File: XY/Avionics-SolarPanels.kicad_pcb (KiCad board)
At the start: 4 copper layers, 82 x 100 mm, 213 parts, among them J1 200528-0100, J2 200528-0100, Q1 NX3008NBKS, Q10 MBT2222ADW1T1, Q11 NX3008NBKS, Q12 MBT2222ADW1T1, Q13 NX3008NBKS, Q14 MBT2222ADW1T1, Q15 NX3008NBKS, Q16 MBT2222ADW1T1, Q2 MBT2222ADW1T1, Q3 NX3008NBKS, Q4 MBT2222ADW1T1, Q5 NX3008NBKS, Q6 MBT2222ADW1T1, Q7 NX3008NBKS, Q8 MBT2222ADW1T1, Q9 NX3008NBKS, U1 OPT4003DNPRQ1, U10 NCV891330PD50R2G, U11 LTC4376CDHD_PBF, U12 LTC3130, U13 LTC4376CDHD_PBF, U14 SI3865DDV-T1-GE3, U2 ADM1176-1ARMZ-R7, U3 LTC3130, U4 LTC3130, U5 DRV8830DRC, U6 ADM1176-1ARMZ-R7, U7 SI3865DDV-T1-GE3, U8 LTC4376CDHD_PBF, U9 SI3865DDV-T1-GE3

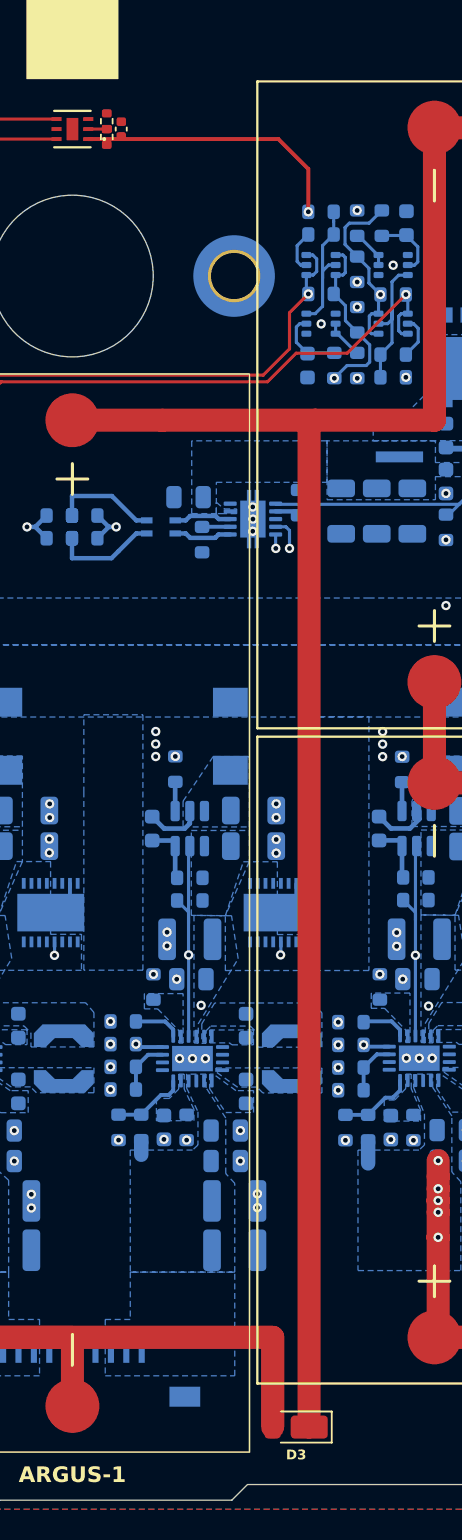
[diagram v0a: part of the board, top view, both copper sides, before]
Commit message: Added Z+ and Z- projects (WIP)
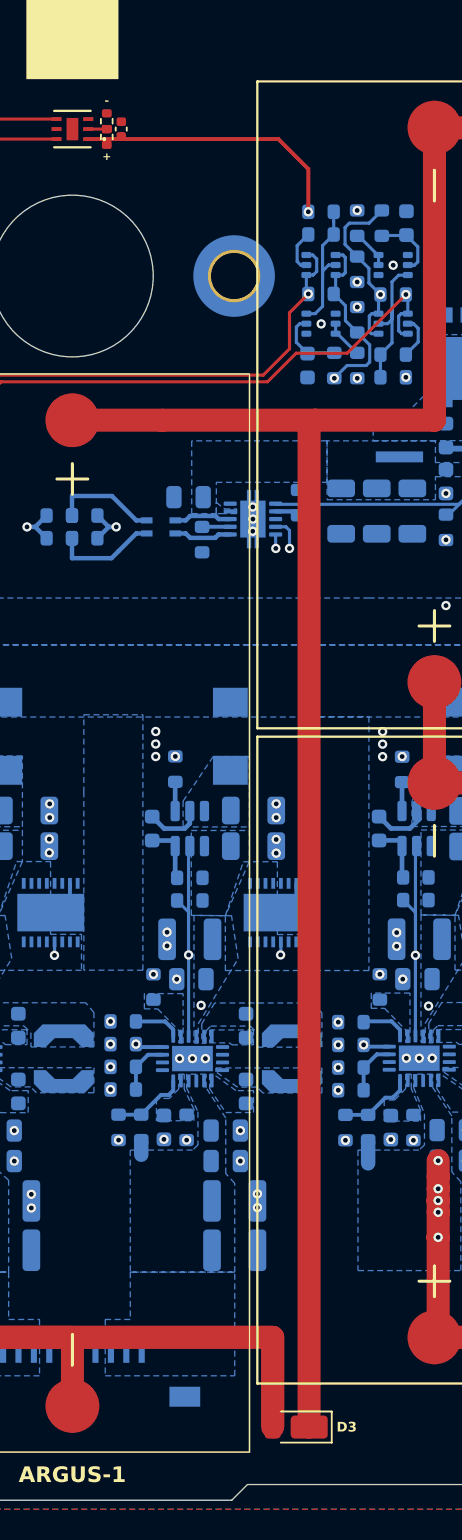
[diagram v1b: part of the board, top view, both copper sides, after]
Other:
- board text added: "+"
- board text added: "-"
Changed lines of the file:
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@@
 		(tags "PowerDI diode vishay")
 		(property "Reference" "D3"
-			(at -0.000001 -1.8034 180)
+			(at -2.6152 0 180)
 			(layer "F.SilkS")
 			(effects
@@
 					(bold yes)
 				)
+				(justify left)
 			)
 		)
@@
 			(pintype "passive")
 		)
-		(model "${KIPRJMOD}/../KiCad-Libraries/3D Models/SM141K06TF.step"
+		(model "${KIPRJMOD}/../../KiCad-Libraries/3D Models/SM141K06TF.step"
 			(offset
 				(xyz 0 0 0)
@@
 			(pintype "power_out")
 		)
-		(model "${KIPRJMOD}/../KiCad-Libraries/3D Models/OPT4003DNPRQ1.STEP"
+		(model "${KIPRJMOD}/../../KiCad-Libraries/3D Models/OPT4003DNPRQ1.STEP"
 			(offset
 				(xyz 0 0 0)
@@
 			(pintype "passive")
 		)
-		(model "${KIPRJMOD}/../KiCad-Libraries/3D Models/SM141K10TF.step"
+		(model "${KIPRJMOD}/../../KiCad-Libraries/3D Models/SM141K10TF.step"
 			(offset
 				(xyz 0 0 0)
@@
 			(pintype "passive")
 		)
-		(model "${KIPRJMOD}/../KiCad-Libraries/3D Models/SM141K06TF.step"
+		(model "${KIPRJMOD}/../../KiCad-Libraries/3D Models/SM141K06TF.step"
 			(offset
 				(xyz 0 0 0)
@@
 			(pintype "passive")
 		)
-		(model "${KIPRJMOD}/../KiCad-Libraries/3D Models/SM141K06TF.step"
+		(model "${KIPRJMOD}/../../KiCad-Libraries/3D Models/SM141K06TF.step"
 			(offset
 				(xyz 0 0 0)
@@
 			(pintype "passive")
 		)
-		(model "${KIPRJMOD}/../KiCad-Libraries/3D Models/SM141K06TF.step"
+		(model "${KIPRJMOD}/../../KiCad-Libraries/3D Models/SM141K06TF.step"
 			(offset
 				(xyz 0 0 0)
@@
 			(pintype "passive")
 		)
-		(model "${KIPRJMOD}/../KiCad-Libraries/3D Models/2005280100.stp"
+		(model "${KIPRJMOD}/../../KiCad-Libraries/3D Models/2005280100.stp"
 			(offset
 				(xyz 0 0 0)
@@
 			(pintype "passive")
 		)
-		(model "${KIPRJMOD}/../KiCad-Libraries/3D Models/srf2012a.stp"
+		(model "${KIPRJMOD}/../../KiCad-Libraries/3D Models/srf2012a.stp"
 			(offset
 				(xyz 0 0 0.6)
@@
 			(pintype "passive")
 		)
-		(model "${KIPRJMOD}/../KiCad-Libraries/3D Models/LSM115JE3_TR13.step"
+		(model "${KIPRJMOD}/../../KiCad-Libraries/3D Models/LSM115JE3_TR13.step"
 			(offset
 				(xyz 0 0 0)
@@
 			(layers "B.Cu" "B.Paste" "B.Mask")
 		)
-		(model "${KIPRJMOD}/../KiCad-Libraries/3D Models/NRVB440MFSWFT3G.step"
+		(model "${KIPRJMOD}/../../KiCad-Libraries/3D Models/NRVB440MFSWFT3G.step"
 			(offset
 				(xyz 0 0 0)
@@
 			(pintype "passive")
 		)
-		(model "${KIPRJMOD}/../KiCad-Libraries/3D Models/XGL3520.step"
+		(model "${KIPRJMOD}/../../KiCad-Libraries/3D Models/XGL3520.step"
 			(offset
 				(xyz 0 0 0)
@@
 			)
 		)
-		(model "${KIPRJMOD}/../KiCad-Libraries/3D Models/Coilcraft-LPS4018.step"
+		(model "${KIPRJMOD}/../../KiCad-Libraries/3D Models/Coilcraft-LPS4018.step"
 			(offset
 				(xyz 0 0 0)
@@
 			)
 		)
-		(model "${KIPRJMOD}/../KiCad-Libraries/3D Models/Coilcraft-LPS4018.step"
+		(model "${KIPRJMOD}/../../KiCad-Libraries/3D Models/Coilcraft-LPS4018.step"
 			(offset
 				(xyz 0 0 0)
@@
 			(pintype "passive")
 		)
-		(model "${KIPRJMOD}/../KiCad-Libraries/3D Models/LSM115JE3_TR13.step"
+		(model "${KIPRJMOD}/../../KiCad-Libraries/3D Models/LSM115JE3_TR13.step"
 			(offset
 				(xyz 0 0 0)
@@
 			)
 		)
-		(model "${KIPRJMOD}/../KiCad-Libraries/3D Models/Coilcraft-LPS4018.step"
+		(model "${KIPRJMOD}/../../KiCad-Libraries/3D Models/Coilcraft-LPS4018.step"
 			(offset
 				(xyz 0 0 0)
@@
 			(pintype "passive")
 		)
-		(model "${KIPRJMOD}/../KiCad-Libraries/3D Models/2005280100.stp"
+		(model "${KIPRJMOD}/../../KiCad-Libraries/3D Models/2005280100.stp"
 			(offset
 				(xyz 0 0 0)
@@
 			(pintype "passive")
 		)
-		(model "${KIPRJMOD}/../KiCad-Libraries/3D Models/LSM115JE3_TR13.step"
+		(model "${KIPRJMOD}/../../KiCad-Libraries/3D Models/LSM115JE3_TR13.step"
 			(offset
 				(xyz 0 0 0)
@@
 			)
 		)
+	)
+	(gr_text "-"
+		(at 154.6352 61.5188 0)
+		(layer "F.SilkS")
+		(effects
+			(font
+				(size 0.508 0.508)
+				(thickness 0.1016)
+				(bold yes)
+			)
+		)
+	)
+	(gr_text "+"
+		(at 154.6352 65.151 0)
+		(layer "F.SilkS")
+		(effects
+			(font
+				(size 0.508 0.508)
+				(thickness 0.1016)
+				(bold yes)
+			)
+		)

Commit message: Z- Board Files
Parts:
- R10, R18, R5: value R_Small -> 107K
- R12, R20, R7: value R_Small -> 1.47M
- R13, R21, R8: value R_Small -> 200K
- R17, R3, R9: value R_Small -> 1.91M
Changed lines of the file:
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@@
 		(pcbplotparams
 			(layerselection 0x00010fc_ffffffff)
-			(plot_on_all_layers_selection 0x0001000_00000000)
+			(plot_on_all_layers_selection 0x0000000_00000000)
 			(disableapertmacros no)
 			(usegerberextensions no)
@@
 		)
 		(property "Footprint" "SolarPanels:OPT4003"
-			(at 0 0 0)
+			(at 0 0 180)
 			(layer "F.Fab")
 			(hide yes)
@@
 		)
 		(property "Datasheet" "OPT4003DNPRQ1"
-			(at 0 0 0)
+			(at 0 0 180)
 			(layer "F.Fab")
 			(hide yes)
@@
 		)
 		(property "Description" ""
-			(at 0 0 0)
+			(at 0 0 180)
 			(layer "F.Fab")
 			(hide yes)
@@
 		)
 		(fp_circle
-			(center -2.0597 -0.65)
-			(end -2.0066 -0.635)
+			(center -1.9558 -1.0414)
+			(end -1.9027 -1.0264)
 			(stroke
 				(width 0.1524)
@@
 			(pintype "power_out")
 		)
-		(model "${KIPRJMOD}/../../KiCad-Libraries/3D Models/OPT4003DNPRQ1.STEP"
+		(model "${KIPRJMOD}/../KiCad-Libraries/3D Models/OPT4003DNPRQ1.STEP"
 			(offset
 				(xyz 0 0 0)
@@
 			)
 		)
-		(property "Value" "R_Small"
+		(property "Value" "1.91M"
 			(at 0 -1.43 90)
 			(layer "B.Fab")
@@
 			)
 		)
-		(property "Value" "R_Small"
+		(property "Value" "1.91M"
 			(at 0 -1.43 90)
 			(layer "B.Fab")
@@
 			)
 		)
-		(property "Value" "R_Small"
+		(property "Value" "1.47M"
 			(at 0 -1.43 0)
 			(layer "B.Fab")
@@
 			)
 		)
-		(property "Value" "R_Small"
+		(property "Value" "107K"
 			(at 0 -1.43 90)
 			(layer "B.Fab")
@@
 			)
 		)
-		(property "Value" "R_Small"
+		(property "Value" "107K"
 			(at 0 -1.43 90)
 			(layer "B.Fab")
@@
 			)
 		)
-		(property "Value" "R_Small"
+		(property "Value" "1.47M"
 			(at 0 -1.43 0)
 			(layer "B.Fab")
@@
 			)
 		)
-		(property "Value" "R_Small"
+		(property "Value" "200K"
 			(at 0 -1.43 0)
 			(layer "B.Fab")
@@
 			)
 		)
-		(property "Value" "R_Small"
+		(property "Value" "1.47M"
 			(at 0 -1.43 0)
 			(layer "B.Fab")
@@
 			)
 		)
-		(property "Value" "R_Small"
+		(property "Value" "200K"
 			(at 0 -1.43 0)
 			(layer "B.Fab")
@@
 			)
 		)
-		(property "Value" "R_Small"
+		(property "Value" "107K"
 			(at 0 -1.43 90)
 			(layer "B.Fab")
@@
 			)
 		)
-		(property "Value" "R_Small"
+		(property "Value" "200K"
 			(at 0 -1.43 0)
 			(layer "B.Fab")
@@
 			)
 		)
-		(property "Value" "R_Small"
+		(property "Value" "1.91M"
 			(at 0 -1.43 90)
 			(layer "B.Fab")

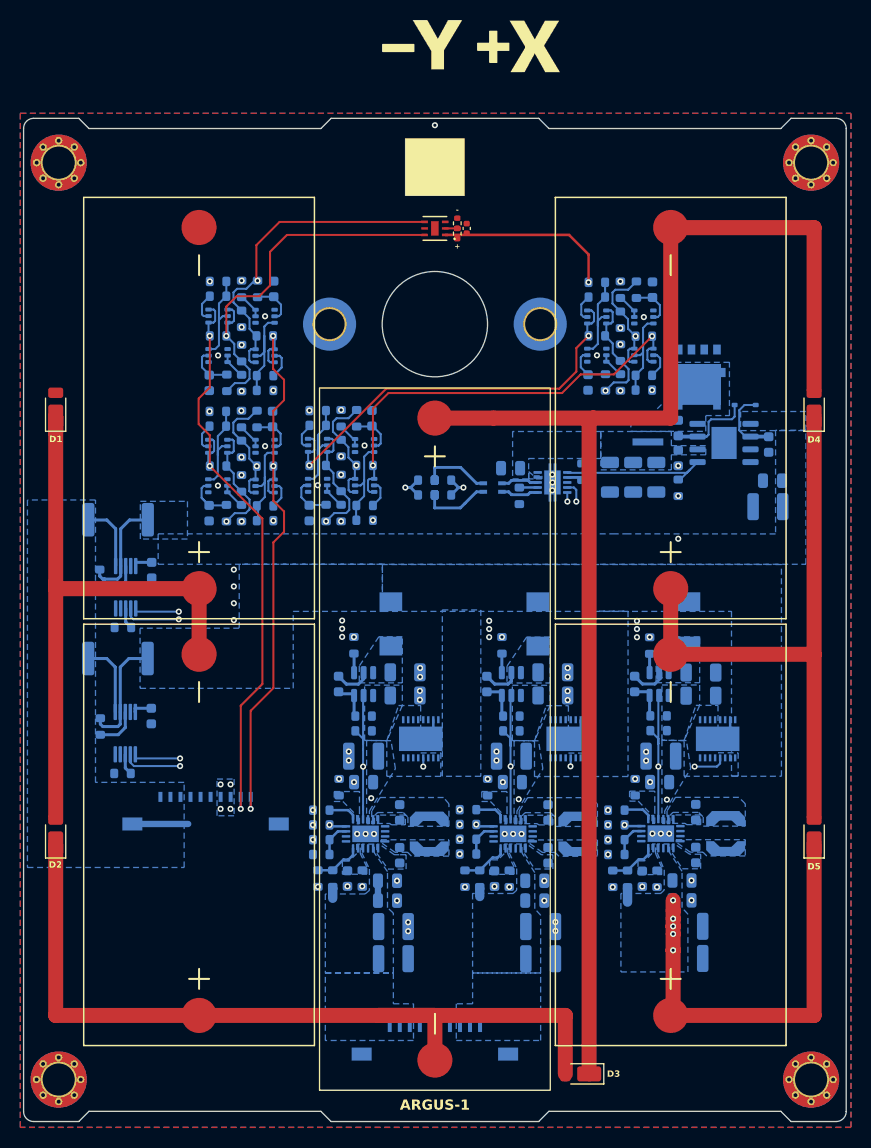
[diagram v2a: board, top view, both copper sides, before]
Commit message: Updated layout
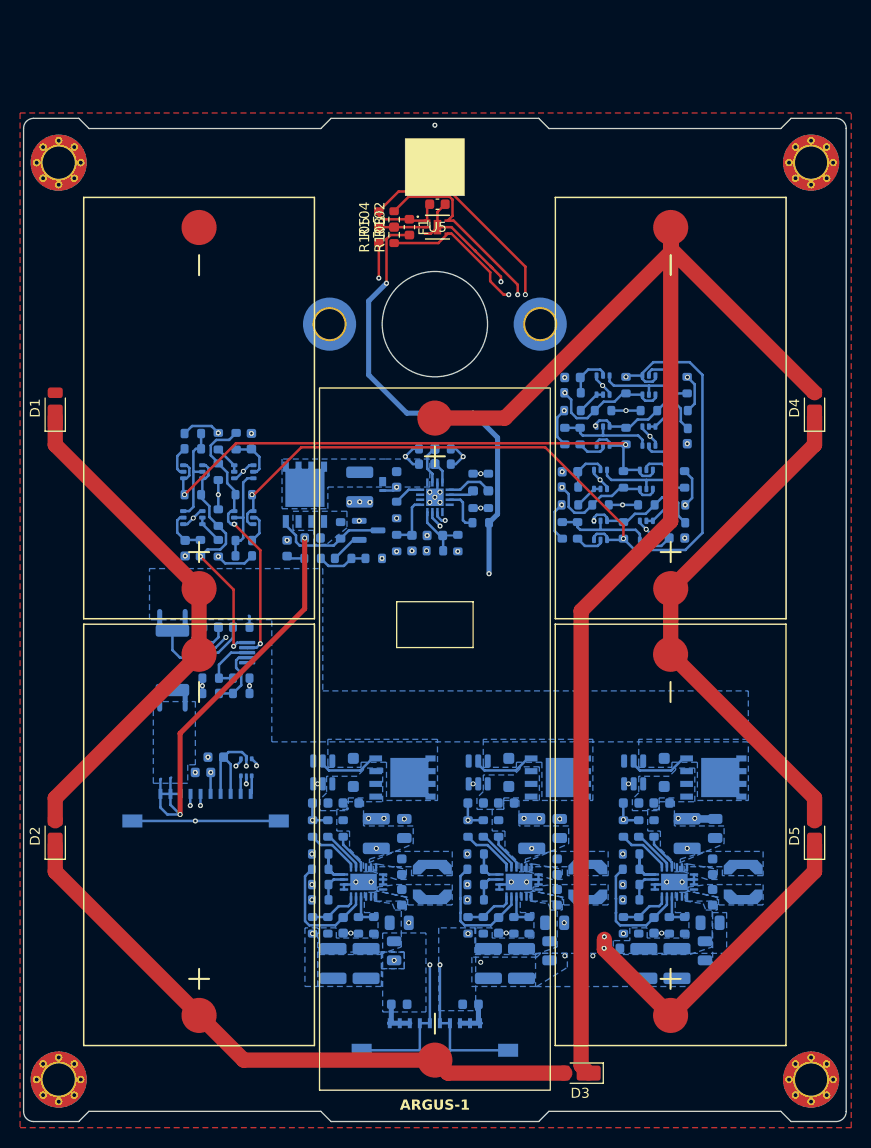
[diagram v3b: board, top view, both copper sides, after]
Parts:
- removed ?: , clipboard:eb50a26b-5fb6-463a-8dd0-ee5887daaa13
- removed C29: 3.3nF, Capacitor_SMD:C_0603_1608Metric
- removed C30, C31, C32, C33: 10nF, Capacitor_SMD:C_0603_1608Metric
- removed C50: 1uF, Capacitor_SMD:C_1206_3216Metric
- removed C51, C52, C53, C54, C55, C56: 1uF, Capacitor_SMD:C_0805_2012Metric
- removed D11: LSM115, SolarPanels:DO-214BA_MCH
- removed FL1: SRF2012, SolarPanels:SRF2012
- removed L4: XGL3520-222, SolarPanels:XGL3520
- removed Q10, Q12, Q14, Q16, Q4, Q6: MBT2222ADW1T1, Package_TO_SOT_SMD:SOT-363_SC-70-6
- removed Q11, Q13, Q15, Q3, Q5, Q9: NX3008NBKS, Package_TO_SOT_SMD:SOT-363_SC-70-6
- removed R40, R41, R47, R55, R56, R58, R65, R66, R70, R71, R75, R76, R80, R81, R91, R93: 10K, Resistor_SMD:R_0603_1608Metric
- removed R42, R57, R59, R67, R72, R77, R82: 200K, Resistor_SMD:R_0603_1608Metric
- removed R43, R63, R68, R73, R78: 680R, Resistor_SMD:R_0603_1608Metric
- removed R44, R45, R83, R84: DNI (0R), Resistor_SMD:R_0603_1608Metric
- removed R46, R64, R69, R74, R79, R90, R92: 100K, Resistor_SMD:R_0603_1608Metric
- removed R61: ?R, Resistor_SMD:R_2512_6332Metric
- removed R62: 1K, Resistor_SMD:R_0603_1608Metric
- removed REF**: , X Label
- removed Ref**: Val**, custom-footprints:ypanel
- removed U14: SI3865DDV-T1-GE3, Package_TO_SOT_SMD:SOT-23-6
- added D8: PMEG4005EH, Diode_SMD:D_SOD-123F, B.Cu at (144.3, 117.6)
- added F1: 100mA, Fuse:Fuse_0603_1608Metric, F.Cu at (149.9, 63.2)
- added F2: 500mA, Fuse:Fuse_0603_1608Metric, B.Cu at (140.2, 94.2)
- added F3: 500mA, Fuse:Fuse_0603_1608Metric, B.Cu at (175.0, 120.7)
- added F4: 500mA, Fuse:Fuse_0603_1608Metric, B.Cu at (159.5, 120.7)
- added F5: 500mA, Fuse:Fuse_0603_1608Metric, B.Cu at (144.0, 120.7)
- added F6: 100mA, Fuse:Fuse_0603_1608Metric, B.Cu at (170.1, 135.1)
- added F7: 100mA, Fuse:Fuse_0603_1608Metric, B.Cu at (156.0, 140.7)
- added F8: 100mA, Fuse:Fuse_0603_1608Metric, B.Cu at (148.8, 140.7)
- added Q17: NX3008NBKS, Package_TO_SOT_SMD:SOT-363_SC-70-6, B.Cu at (173.5, 93.5)
- added Q18: MBT2222ADW1T1, Package_TO_SOT_SMD:SOT-363_SC-70-6, B.Cu at (168.9, 93.5)
- added Q19: NX3008NBKS, Package_TO_SOT_SMD:SOT-363_SC-70-6, B.Cu at (169.2, 79.0)
- added Q20: MBT2222ADW1T1, Package_TO_SOT_SMD:SOT-363_SC-70-6, B.Cu at (173.7, 79.0)
- added Q21: NX3008NBKS, Package_TO_SOT_SMD:SOT-363_SC-70-6, B.Cu at (173.7, 84.1)
- added Q22: MBT2222ADW1T1, Package_TO_SOT_SMD:SOT-363_SC-70-6, B.Cu at (169.2, 84.1)
- added Q23: NX3008NBKS, Package_TO_SOT_SMD:SOT-363_SC-70-6, B.Cu at (133.3, 87.6)
- added Q24: MBT2222ADW1T1, Package_TO_SOT_SMD:SOT-363_SC-70-6, B.Cu at (133.3, 92.2)
- added Q25: NX3008NBKS, Package_TO_SOT_SMD:SOT-363_SC-70-6, B.Cu at (128.3, 92.2)
- added Q26: MBT2222ADW1T1, Package_TO_SOT_SMD:SOT-363_SC-70-6, B.Cu at (128.3, 87.6)
- added R100: 10K, Resistor_SMD:R_0603_1608Metric, B.Cu at (173.5, 90.9)
- added R101: 200K, Resistor_SMD:R_0603_1608Metric, B.Cu at (176.5, 92.7)
- added R102: 0R, Resistor_SMD:R_0603_1608Metric, F.Cu at (148.3, 62.5)
- added R103: 0R, Resistor_SMD:R_0603_1608Metric, F.Cu at (148.3, 64.0)
- added R104: 0R, Resistor_SMD:R_0603_1608Metric, F.Cu at (146.8, 62.5)
- added R105: 0R, Resistor_SMD:R_0603_1608Metric, F.Cu at (146.8, 64.0)
- added R106: 680R, Resistor_SMD:R_0603_1608Metric, B.Cu at (176.0, 79.0)
- added R107: 100K, Resistor_SMD:R_0603_1608Metric, B.Cu at (166.1, 81.5)
- added R108: 1.47M, Resistor_SMD:R_0603_1608Metric, B.Cu at (141.0, 128.8)
- added R109: 200K, Resistor_SMD:R_0603_1608Metric, B.Cu at (141.0, 130.3)
- added R110: 0R, Resistor_SMD:R_0603_1608Metric, B.Cu at (133.1, 108.2)
- added R111: 0R, Resistor_SMD:R_0603_1608Metric, B.Cu at (130.0, 108.2)
- added R112: 0R, Resistor_SMD:R_0603_1608Metric, B.Cu at (133.1, 109.7)
- added R113: 0R, Resistor_SMD:R_0603_1608Metric, B.Cu at (130.0, 109.7)
- added R114: DNI (0R), Resistor_SMD:R_0603_1608Metric, B.Cu at (171.4, 79.0)
- added R115: 10K, Resistor_SMD:R_0603_1608Metric, B.Cu at (177.5, 79.0)
- added R116: 10K, Resistor_SMD:R_0603_1608Metric, B.Cu at (169.2, 81.5)
- added R117: 200K, Resistor_SMD:R_0603_1608Metric, B.Cu at (166.1, 79.8)
- added R118: 680R, Resistor_SMD:R_0603_1608Metric, B.Cu at (166.9, 84.1)
- added R119: 100K, Resistor_SMD:R_0603_1608Metric, B.Cu at (176.8, 81.5)
- added R120: DNI (0R), Resistor_SMD:R_0603_1608Metric, B.Cu at (171.4, 84.1)
- added R121: 10K, Resistor_SMD:R_0603_1608Metric, B.Cu at (165.4, 84.1)
- added R122: 10K, Resistor_SMD:R_0603_1608Metric, B.Cu at (173.7, 81.5)
- added R123: 200K, Resistor_SMD:R_0603_1608Metric, B.Cu at (176.8, 83.3)
- added R124: ?R, Resistor_SMD:R_2512_6332Metric, B.Cu at (126.2, 106.4)
- added R125: 1K, Resistor_SMD:R_0603_1608Metric, B.Cu at (133.1, 103.1)
- added R126: 680R, Resistor_SMD:R_0603_1608Metric, B.Cu at (133.3, 94.5)
- added R127: 100K, Resistor_SMD:R_0603_1608Metric, B.Cu at (130.8, 84.6)
- added R128: DNI (0R), Resistor_SMD:R_0603_1608Metric, B.Cu at (133.3, 89.9)
- added R129: 10K, Resistor_SMD:R_0603_1608Metric, B.Cu at (133.3, 96.0)
- added R130: 10K, Resistor_SMD:R_0603_1608Metric, B.Cu at (130.8, 87.6)
- added R131: 200K, Resistor_SMD:R_0603_1608Metric, B.Cu at (132.6, 84.6)
- added R132: 680R, Resistor_SMD:R_0603_1608Metric, B.Cu at (128.3, 85.3)
- added R133: 100K, Resistor_SMD:R_0603_1608Metric, B.Cu at (130.8, 95.2)
- added R134: DNI (0R), Resistor_SMD:R_0603_1608Metric, B.Cu at (128.3, 89.9)
- added R135: 10K, Resistor_SMD:R_0603_1608Metric, B.Cu at (128.3, 83.8)
- added R136: 10K, Resistor_SMD:R_0603_1608Metric, B.Cu at (130.8, 92.2)
- added R137: 200K, Resistor_SMD:R_0603_1608Metric, B.Cu at (129.0, 95.2)
- added R97: 100K, Resistor_SMD:R_0603_1608Metric, B.Cu at (176.5, 90.9)
- added R98: DNI (0R), Resistor_SMD:R_0603_1608Metric, B.Cu at (171.2, 93.5)
- added R99: 10K, Resistor_SMD:R_0603_1608Metric, B.Cu at (165.1, 93.5)
- C1: value 47uF -> 0.1uF; footprint Capacitor_SMD:C_1210_3225Metric -> Capacitor_SMD:C_0603_1608Metric
- C10: value 1uF -> 4.7uF; footprint Capacitor_SMD:C_0805_2012Metric -> Capacitor_SMD:C_0603_1608Metric
- C11: value 22nF -> 1uF; footprint Capacitor_SMD:C_0603_1608Metric -> Capacitor_SMD:C_0805_2012Metric
- C12, C4: value 22nF -> 47uF; footprint Capacitor_SMD:C_0603_1608Metric -> Capacitor_SMD:C_1210_3225Metric
- C13: value 4.7uF -> 47uF; footprint Capacitor_SMD:C_0603_1608Metric -> Capacitor_SMD:C_1210_3225Metric
- C14: value 47uF -> 10uF
- C15, C7: value 47uF -> 1uF; footprint Capacitor_SMD:C_1210_3225Metric -> Capacitor_SMD:C_0805_2012Metric
- C16: value 10uF -> 1uF; footprint Capacitor_SMD:C_1210_3225Metric -> Capacitor_SMD:C_0805_2012Metric
- C17: value 1uF -> 22nF; footprint Capacitor_SMD:C_0805_2012Metric -> Capacitor_SMD:C_0603_1608Metric
- C19: value 22nF -> 4.7uF
- C2: value 10uF -> 0.1uF; footprint Capacitor_SMD:C_1210_3225Metric -> Capacitor_SMD:C_0603_1608Metric
- C20, C6: value 4.7uF -> 1uF; footprint Capacitor_SMD:C_0603_1608Metric -> Capacitor_SMD:C_0805_2012Metric
- C22: value 3.3nF -> 1nF
- C23: value 0.1uF -> 47uF; footprint Capacitor_SMD:C_0402_1005Metric -> Capacitor_SMD:C_1210_3225Metric; moved to B.Cu
- C24, C25: value 10nF -> 100nF
- C26: value 10nF -> 10uF; footprint Capacitor_SMD:C_0603_1608Metric -> Capacitor_SMD:C_1210_3225Metric
- C27: value 10nF -> 0.1uF
- C28: footprint Capacitor_SMD:C_0805_2012Metric -> Capacitor_SMD:C_0603_1608Metric
- C3: value 1uF -> 0.1uF; footprint Capacitor_SMD:C_0805_2012Metric -> Capacitor_SMD:C_0603_1608Metric
- C34: value 1uF -> 10nF; footprint Capacitor_SMD:C_0805_2012Metric -> Capacitor_SMD:C_0603_1608Metric
- C35: value 4.7uF -> 10nF; footprint Capacitor_SMD:C_1210_3225Metric -> Capacitor_SMD:C_0603_1608Metric
- C36: moved to F.Cu
- C37: value 0.1uF -> 10nF
- C38, C48: value 10uF -> 10nF; footprint Capacitor_SMD:C_1206_3216Metric -> Capacitor_SMD:C_0603_1608Metric
- C39: value 0.1uF -> 10uF; footprint Capacitor_SMD:C_0603_1608Metric -> Capacitor_SMD:C_1210_3225Metric
- C40, C41, C45: value 10uF -> 1uF; footprint Capacitor_SMD:C_1206_3216Metric -> Capacitor_SMD:C_0805_2012Metric
- C42: value 10uF -> 22nF; footprint Capacitor_SMD:C_1206_3216Metric -> Capacitor_SMD:C_0603_1608Metric
- C43: value 1nF -> 22nF
- C44: value 1uF -> 4.7uF; footprint Capacitor_SMD:C_1206_3216Metric -> Capacitor_SMD:C_0603_1608Metric
- C46: value 1nF -> 47uF; footprint Capacitor_SMD:C_0603_1608Metric -> Capacitor_SMD:C_1210_3225Metric
- C47: value 1uF -> 3.3nF; footprint Capacitor_SMD:C_1206_3216Metric -> Capacitor_SMD:C_0603_1608Metric
- C49: value 1nF -> 10nF
- C5: value 22nF -> 10uF; footprint Capacitor_SMD:C_0603_1608Metric -> Capacitor_SMD:C_1210_3225Metric
- C8: value 47uF -> 22nF; footprint Capacitor_SMD:C_1210_3225Metric -> Capacitor_SMD:C_0603_1608Metric
- C9: value 10uF -> 22nF; footprint Capacitor_SMD:C_1210_3225Metric -> Capacitor_SMD:C_0603_1608Metric
- D10: value NRVB440MFS -> 10V; footprint SolarPanels:NRVB440MFSWFT1G -> Diode_SMD:Nexperia_DSN1608-2_1.6x0.8mm
- D6, D7: value LSM115 -> PMEG4005EH; footprint SolarPanels:DO-214BA_MCH -> Diode_SMD:D_SOD-123F
- D9: value BAS16HT1G -> GREEN; footprint Diode_SMD:D_SOD-323 -> LED_SMD:LED_0603_1608Metric
- Q1: value NX3008NBKS -> IRLML2803; footprint Package_TO_SOT_SMD:SOT-363_SC-70-6 -> Package_TO_SOT_SMD:SOT-23
- Q2: value MBT2222ADW1T1 -> SIRA99DP-T1-GE3; footprint Package_TO_SOT_SMD:SOT-363_SC-70-6 -> Package_SO:PowerPAK_SO-8_Single
- R1: value 0R -> 0R (DNI)
- R10: value 107K -> 0R
- R11, R49, R54, R6: value 100K -> 0R
- R12, R7: value 1.47M -> 0R
- R13: value 200K -> 1.91M
- R14: value 0R (DNI) -> 1.91M
- R15, R16: value 0R -> 1.91M
- R17: value 1.91M -> 107K
- R18: value 107K -> 1.91M
- R19: value 100K -> 107K
- R2: value 0R (DNI) -> 0R
- R20: value 1.47M -> 1.91M
- R21: value 200K -> 107K
- R22: value 0R (DNI) -> 127k
- R23, R24: value 0R -> 127k
- R25, R26, R27: value 0R -> 100K
- R3: value 1.91M -> 0R
- R32: value ?R -> TBD; footprint Resistor_SMD:R_2512_6332Metric -> Resistor_SMD:R_0603_1608Metric
- R33: value 1K -> 10k
- R34: value 0R -> 1.47M; footprint Resistor_SMD:R_0402_1005Metric -> Resistor_SMD:R_0603_1608Metric; moved to B.Cu
- R35: value 0R -> 200K; footprint Resistor_SMD:R_0402_1005Metric -> Resistor_SMD:R_0603_1608Metric; moved to B.Cu
- R36: value 680R -> 2.7k
- R37: value 100K -> 10k
- R38: value DNI (0R) -> 10k
- R39: value DNI (0R) -> 4k7
- R48: value 680R -> 0R
- R5: value 107K -> 0R (DNI)
- R50, R51: value 10K -> 0R
- R52: value 200K -> TBD
- R53: value 680R -> TBD
- R60, R96: value 0R -> 680R
- R8: value 200K -> 0R
- R85: value DNI (0R) -> 100K
- R86: value DNI (0R) -> 10K
- R88: value 100K -> 1.47M
- R89: value 10K -> 200K
- R9: value 1.91M -> 0R (DNI)
- R94: value 0R -> 200K
- R95: value 0R -> DNI (0R)
- U1: value OPT4003DNPRQ1 -> LTC4412xS6; footprint SolarPanels:OPT4003 -> Package_TO_SOT_SMD:TSOT-23-6; moved to B.Cu
- U10: value NCV891330PD50R2G -> LTC3130; footprint Package_SO:SOIC-8-1EP_3.9x4.9mm_P1.27mm_EP2.514x3.2mm -> Package_DFN_QFN:QFN-20-1EP_3x4mm_P0.5mm_EP1.65x2.65mm
- U11: value LTC4376CDHD_PBF -> LTC3130; footprint Package_DFN_QFN:DFN-16-1EP_4x5mm_P0.5mm_EP2.44x4.34mm -> Package_DFN_QFN:QFN-20-1EP_3x4mm_P0.5mm_EP1.65x2.65mm
- U13: value LTC4376CDHD_PBF -> ADM1176-1ARMZ-R7; footprint Package_DFN_QFN:DFN-16-1EP_4x5mm_P0.5mm_EP2.44x4.34mm -> Package_SO:MSOP-10_3x3mm_P0.5mm
- U2: value ADM1176-1ARMZ-R7 -> DRV8235RTER; footprint Package_SO:MSOP-10_3x3mm_P0.5mm -> SolarPanels:WQFN16_RTE_TEX
- U3: value LTC3130 -> CSD25402Q3A; footprint Package_DFN_QFN:QFN-20-1EP_3x4mm_P0.5mm_EP1.65x2.65mm -> Package_SO:PowerPAK_SO-8_Single
- U4: value LTC3130 -> LTC4412xS6; footprint Package_DFN_QFN:QFN-20-1EP_3x4mm_P0.5mm_EP1.65x2.65mm -> Package_TO_SOT_SMD:TSOT-23-6
- U5: value DRV8830DRC -> OPT4003DNPRQ1; footprint Package_SON:VSON-10-1EP_3x3mm_P0.5mm_EP1.65x2.4mm -> SolarPanels:OPT4003; moved to F.Cu
- U6: value ADM1176-1ARMZ-R7 -> USBLC6-2P6; footprint Package_SO:MSOP-10_3x3mm_P0.5mm -> Package_TO_SOT_SMD:SOT-666
- U7, U9: value SI3865DDV-T1-GE3 -> CSD25402Q3A; footprint Package_TO_SOT_SMD:SOT-23-6 -> Package_SO:PowerPAK_SO-8_Single
- U8: value LTC4376CDHD_PBF -> LTC4412xS6; footprint Package_DFN_QFN:DFN-16-1EP_4x5mm_P0.5mm_EP2.44x4.34mm -> Package_TO_SOT_SMD:TSOT-23-6
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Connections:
- net /coil renamed /Coil Driver/coil
- C1 pad 1: VSOLAR -> Net-(D6-A)
- C10 pad 1: D_VSOLAR1 -> /Solar Charger/MPPT/VCC
- C11 pad 1: Net-(U3-SW1) -> /Solar Charger/Charge OR-ing/IN
- C11 pad 2: Net-(U3-BST1) -> GND
- C12 pad 1: Net-(U3-BST2) -> /Solar Charger/Charge OR-ing/IN
- C12 pad 2: Net-(U3-SW2) -> GND
- C13 pad 1: /MPPT1/VCC -> /Solar Charger/MPPT1/VIN
- C14 pad 1: /Charge OR-ing1/IN -> /Solar Charger/MPPT1/VIN
- C15 pad 1: D_VSOLAR2 -> /Solar Charger/MPPT1/VIN
- C16 pad 1: D_VSOLAR2 -> /Solar Charger/MPPT1/VIN
- C17 pad 1: D_VSOLAR2 -> Net-(U11-SW1)
- C17 pad 2: GND -> Net-(U11-BST1)
- C18 pad 1: Net-(U4-SW1) -> Net-(U11-BST2)
- C18 pad 2: Net-(U4-BST1) -> Net-(U11-SW2)
- C19 pad 1: Net-(U4-BST2) -> /Solar Charger/MPPT1/VCC
- C19 pad 2: Net-(U4-SW2) -> GND
- C2 pad 1: VSOLAR -> Net-(D7-A)
- C20 pad 1: /MPPT2/VCC -> /Solar Charger/Charge OR-ing1/IN
- C21 pad 1: /Charge OR-ing2/IN -> /Solar Charger/Charge OR-ing1/IN
- C22 pad 1: GND -> /Coil Driver/IPROPI
- C22 pad 2: Net-(U2-TIMER) -> GND
- C23 pad 1: 3.3V -> /Solar Charger/MPPT2/VIN
- C24 pad 1: Net-(Q1B-G1) -> MAIN_3V3
- C25 pad 1: Net-(Q3B-G1) -> PERI_3V3
- C26 pad 1: Net-(Q5B-G1) -> /Coil Driver/VM
- C27 pad 1: Net-(Q7B-G1) -> /Coil Driver/VM
- C28 pad 1: +5V -> /Coil Driver/VREF
- C3 pad 1: VSOLAR -> Net-(D8-A)
- C34 pad 1: GND -> Net-(Q7B-G1)
- C34 pad 2: VDRIVE -> GND
- C35 pad 1: GND -> Net-(Q17B-G1)
- C35 pad 2: VDRIVE -> GND
- C36 pad 1: GND -> /Light Sensor/LS_3V3
- C36 pad 2: Net-(D9-A) -> GND
- C37 pad 1: Net-(D9-K) -> Net-(Q19B-G1)
- C37 pad 2: Net-(D10-K) -> GND
- C38 pad 1: GND -> Net-(Q21B-G1)
- C38 pad 2: +5V -> GND
- C39 pad 1: GND -> /Solar Charger/MPPT2/VIN
- C39 pad 2: +5V -> GND
- C4 pad 1: Net-(U12-SW1) -> /Solar Charger/VSOLAR
- C4 pad 2: Net-(U12-BST1) -> GND
- C40 pad 1: GND -> /Solar Charger/MPPT2/VIN
- C40 pad 2: +5V -> GND
- C41 pad 1: GND -> /Solar Charger/MPPT2/VIN
- C41 pad 2: +5V -> GND
- C42 pad 1: /Charge OR-ing/IN -> Net-(U12-SW1)
- C42 pad 2: GND -> Net-(U12-BST1)
- C43 pad 1: Net-(U14-R1,C1) -> Net-(U12-BST2)
- C43 pad 2: Net-(D11-A) -> Net-(U12-SW2)
- C44 pad 1: Net-(D11-A) -> /Solar Charger/MPPT2/VCC
- C45 pad 1: /Charge OR-ing1/IN -> /Solar Charger/Charge OR-ing2/IN
- C46 pad 1: Net-(U7-R1,C1) -> /Solar Charger/Charge OR-ing2/IN
- C46 pad 2: Net-(D6-A) -> GND
- C47 pad 1: Net-(D6-A) -> GND
- C47 pad 2: GND -> Net-(U13-TIMER)
- C48 pad 1: /Charge OR-ing2/IN -> Net-(Q23B-G1)
- C49 pad 1: Net-(U9-R1,C1) -> Net-(Q25B-G1)
- C49 pad 2: Net-(D7-A) -> GND
- C5 pad 1: Net-(U12-BST2) -> /Solar Charger/VSOLAR
- C5 pad 2: Net-(U12-SW2) -> GND
- C6 pad 1: /MPPT/VCC -> /Solar Charger/VSOLAR
- C7 pad 1: /Charge OR-ing/IN -> /Solar Charger/VSOLAR
- C8 pad 1: D_VSOLAR1 -> Net-(U10-SW1)
- C8 pad 2: GND -> Net-(U10-BST1)
- C9 pad 1: D_VSOLAR1 -> Net-(U10-BST2)
- C9 pad 2: GND -> Net-(U10-SW2)
- D10 pad 1: Net-(D10-K) -> /Coil Driver/VM
- D5 pad 1: VSOLAR -> Net-(D5-K)
- D6 pad 1: VCHRG -> /Solar Charger/VCHRG
- D7 pad 1: VCHRG -> /Solar Charger/VCHRG
- D9 pad 1: Net-(D9-K) -> GND
- J2 pad 1: SCL -> Net-(J2-Pin_1)
- J2 pad 2: SDA -> Net-(J2-Pin_2)
- J2 pad 3: 3.3V -> MAIN_3V3
- J2 pad 4: 3.3V -> MAIN_3V3
- J2 pad 5: GND -> PERI_3V3
- L1 pad 1: Net-(U12-SW1) -> Net-(U10-SW1)
- L1 pad 2: Net-(U12-SW2) -> Net-(U10-SW2)
- L2 pad 1: Net-(U3-SW1) -> Net-(U11-SW1)
- L2 pad 2: Net-(U3-SW2) -> Net-(U11-SW2)
- L3 pad 1: Net-(U4-SW1) -> Net-(U12-SW1)
- L3 pad 2: Net-(U4-SW2) -> Net-(U12-SW2)
- Q1 pad 1: GND -> Net-(Q1-G)
- Q1 pad 2: Net-(Q1A-G2) -> GND
- Q1 pad 3: Net-(Q1A-G2) -> Net-(Q1-D)
- Q2 pad 1: SCL -> Net-(F2-Pad1)
- Q2 pad 2: Net-(Q2A-B1) -> Net-(F2-Pad1)
- Q2 pad 3: SCL -> Net-(F2-Pad1)
- Q2 pad 4: SCL_LS -> Net-(Q1-D)
- Q2 pad 5: Net-(Q1A-D1) -> /Coil Driver/VM
- Q8 pad 1: SDA -> SCL
- Q8 pad 3: SDA -> SCL
- Q8 pad 4: SDA_CPWR -> /Coil Driver/SCL_M
- Q8 pad 6: SDA_CPWR -> /Coil Driver/SCL_M
- R1 pad 1: Net-(U12-ILIM) -> Net-(U10-ILIM)
- R1 pad 2: GND -> /Solar Charger/MPPT/VCC
- R10 pad 1: /MPPT1/MPPC -> Net-(U12-ILIM)
- R11 pad 1: /PGOOD2 -> Net-(U12-MODE)
- R11 pad 2: /Charge OR-ing1/IN -> GND
- R12 pad 1: /Charge OR-ing1/IN -> GND
- R12 pad 2: /MPPT1/FB -> Net-(U12-EXTVCC)
- R13 pad 1: /MPPT1/FB -> /Solar Charger/VSOLAR
- R13 pad 2: GND -> /Solar Charger/MPPT/RUN
- R14 pad 1: Net-(U3-ILIM) -> /Solar Charger/MPPT1/VIN
- R14 pad 2: /MPPT1/VCC -> /Solar Charger/MPPT1/RUN
- R15 pad 1: Net-(U3-ILIM) -> /Solar Charger/MPPT2/VIN
- R15 pad 2: GND -> /Solar Charger/MPPT2/RUN
- R16 pad 1: GND -> /Solar Charger/VSOLAR
- R16 pad 2: Net-(U3-EXTVCC) -> /Solar Charger/MPPT/MPPC
- R17 pad 1: D_VSOLAR2 -> /Solar Charger/MPPT/MPPC
- R17 pad 2: /MPPT2/MPPC -> GND
- R18 pad 1: /MPPT2/MPPC -> /Solar Charger/MPPT1/VIN
- R18 pad 2: GND -> /Solar Charger/MPPT1/MPPC
- R19 pad 1: /PGOOD3 -> /Solar Charger/MPPT1/MPPC
- R19 pad 2: /Charge OR-ing2/IN -> GND
- R2 pad 1: Net-(U12-ILIM) -> Net-(U10-ILIM)
- R2 pad 2: /MPPT/VCC -> GND
- R20 pad 1: /Charge OR-ing2/IN -> /Solar Charger/MPPT2/VIN
- R20 pad 2: /MPPT2/FB -> /Solar Charger/MPPT2/MPPC
- R21 pad 1: /MPPT2/FB -> /Solar Charger/MPPT2/MPPC
- R22 pad 1: Net-(U4-ILIM) -> /Solar Charger/MPPT/RUN
- R22 pad 2: /MPPT2/VCC -> GND
- R23 pad 1: Net-(U4-ILIM) -> /Solar Charger/MPPT1/RUN
- R24 pad 1: GND -> /Solar Charger/MPPT2/RUN
- R24 pad 2: Net-(U4-EXTVCC) -> GND
- R25 pad 1: Net-(U12-MODE) -> /Solar Charger/PGOOD1
- R25 pad 2: GND -> /Solar Charger/Charge OR-ing/IN
- R26 pad 1: Net-(U3-MODE) -> /Solar Charger/PGOOD2
- R26 pad 2: GND -> /Solar Charger/Charge OR-ing1/IN
- R27 pad 1: Net-(U4-MODE) -> /Solar Charger/PGOOD3
- R27 pad 2: GND -> /Solar Charger/Charge OR-ing2/IN
- R3 pad 1: VSOLAR -> Net-(U10-MODE)
- R3 pad 2: /MPPT/MPPC -> GND
- R32 pad 1: VDRIVE -> /Coil Driver/IPROPI
- R32 pad 2: VBATT -> GND
- R33 pad 1: VDRIVE -> MAIN_3V3
- R33 pad 2: Net-(U2-ON) -> Net-(U2-NFAULT)
- R34 pad 1: Net-(U1-ADDR) -> /Solar Charger/Charge OR-ing/IN
- R34 pad 2: 3.3V -> /Solar Charger/MPPT/FB
- R35 pad 1: GND -> /Solar Charger/MPPT/FB
- R35 pad 2: Net-(U1-ADDR) -> GND
- R36 pad 1: Net-(Q2A-B1) -> COIL_DRIVER_EN
- R36 pad 2: Net-(Q1A-D1) -> Net-(D9-A)
- R37 pad 1: 3.3V -> GND
- R37 pad 2: Net-(Q1A-G2) -> COIL_DRIVER_EN
- R38 pad 1: SCL_LS -> Net-(Q1-D)
- R38 pad 2: SCL -> Net-(F2-Pad1)
- R39 pad 1: SDA_LS -> COIL_DRIVER_EN
- R39 pad 2: SDA -> Net-(Q1-G)
- R4 pad 2: Net-(U12-EXTVCC) -> Net-(U10-EXTVCC)
- R48 pad 1: Net-(Q6A-B1) -> /Coil Driver/A0_COIL
- R48 pad 2: Net-(Q5A-D1) -> MAIN_3V3
- R49 pad 1: 3.3V -> GND
- R49 pad 2: Net-(Q5A-G2) -> /Coil Driver/A0_COIL
- R5 pad 1: /MPPT/MPPC -> Net-(U11-ILIM)
- R5 pad 2: GND -> /Solar Charger/MPPT1/VCC
- R50 pad 1: 3.3V -> /Coil Driver/A1_COIL
- R50 pad 2: Net-(Q5A-D1) -> MAIN_3V3
- R51 pad 1: 3.3V -> GND
- R51 pad 2: SCL_CPWR -> /Coil Driver/A1_COIL
- R52 pad 1: SCL_CPWR -> MAIN_3V3
- R52 pad 2: Net-(Q5B-G1) -> /Coil Driver/VREF
- R53 pad 1: Net-(Q8A-B1) -> /Coil Driver/VREF
- R53 pad 2: Net-(Q7A-D1) -> GND
- R54 pad 1: 3.3V -> Net-(U2-NSLEEP)
- R54 pad 2: Net-(Q7A-G2) -> PERI_3V3
- R6 pad 1: /PGOOD1 -> Net-(U11-ILIM)
- R6 pad 2: /Charge OR-ing/IN -> GND
- R60 pad 1: GND -> Net-(Q8A-B1)
- R60 pad 2: Net-(U5-ISENSE) -> Net-(Q7A-D1)
- R7 pad 1: /Charge OR-ing/IN -> Net-(U11-MODE)
- R7 pad 2: /MPPT/FB -> GND
- R8 pad 1: /MPPT/FB -> GND
- R8 pad 2: GND -> Net-(U11-EXTVCC)
- R85 pad 1: SCL_CPWR -> MAIN_3V3
- R85 pad 2: SCL -> Net-(Q7A-G2)
- R86 pad 1: SDA_CPWR -> MAIN_3V3
- R86 pad 2: SDA -> Net-(Q7A-D1)
- R87 pad 1: M_FAULT -> MAIN_3V3
- R87 pad 2: VDRIVE -> /Coil Driver/SCL_M
- R88 pad 1: Net-(U14-R1,C1) -> /Solar Charger/Charge OR-ing1/IN
- R88 pad 2: /Charge OR-ing/IN -> /Solar Charger/MPPT1/FB
- R89 pad 1: Net-(U14-R2) -> /Solar Charger/MPPT1/FB
- R9 pad 1: D_VSOLAR1 -> Net-(U12-ILIM)
- R9 pad 2: /MPPT1/MPPC -> /Solar Charger/MPPT2/VCC
- R94 pad 1: GND -> /Coil Driver/SCL_M
- R94 pad 2: Net-(U2-A0) -> Net-(Q7B-G1)
- R95 pad 1: GND -> /Coil Driver/SCL_M
- R95 pad 2: Net-(U6-A0) -> SCL
- R96 pad 1: GND -> Net-(Q18A-B1)
- R96 pad 2: Net-(U5-A0) -> Net-(Q17A-D1)
- SC5 pad 1: VSOLAR -> Net-(D5-K)
- U1 pad 1: 3.3V -> Net-(D6-A)
- U1 pad 2: Net-(U1-ADDR) -> GND
- U1 pad 4: SCL_LS -> unconnected-(U1-STAT-Pad4)
- U1 pad 5: unconnected-(U1-INT-Pad5) -> Net-(U1-GATE)
- U1 pad 6: SDA_LS -> /Solar Charger/VCHRG
- U10 pad 1: VDRIVE -> Net-(U10-BST1)
- U10 pad 2: Net-(D9-A) -> /Solar Charger/VSOLAR
- U10 pad 3: unconnected-(U10-RSTB-Pad3) -> /Solar Charger/VSOLAR
- U10 pad 4: GND -> /Solar Charger/MPPT/RUN
- U10 pad 5: M_FAULT -> /Solar Charger/MPPT/VCC
- U10 pad 6: +5V -> /Solar Charger/MPPT/MPPC
- U10 pad 7: Net-(D9-K) -> GND
- U10 pad 8: Net-(D10-K) -> GND
- U10 pad 9: GND -> /Solar Charger/MPPT/FB
- U11 pad 1: /Charge OR-ing/IN -> Net-(U11-BST1)
- U11 pad 10: /Charge OR-ing/IN -> Net-(U11-ILIM)
- U11 pad 11: (no net) -> Net-(U11-MODE)
- U11 pad 12: /PGOOD1 -> Net-(U11-EXTVCC)
- U11 pad 13: /Charge OR-ing/IN -> /Solar Charger/PGOOD2
- U11 pad 14: /Charge OR-ing/IN -> /Solar Charger/Charge OR-ing1/IN
- U11 pad 15: /Charge OR-ing/IN -> Net-(U11-SW2)
- U11 pad 16: /Charge OR-ing/IN -> Net-(U11-BST2)
- U11 pad 17: VCHRG -> GND
- U11 pad 2: /Charge OR-ing/IN -> /Solar Charger/MPPT1/VIN
- U11 pad 3: /Charge OR-ing/IN -> /Solar Charger/MPPT1/VIN
- U11 pad 4: /Charge OR-ing/IN -> /Solar Charger/MPPT1/RUN
- U11 pad 5: (no net) -> /Solar Charger/MPPT1/VCC
- U11 pad 6: GND -> /Solar Charger/MPPT1/MPPC
- U11 pad 7: VCHRG -> GND
- U11 pad 8: unconnected-(U11-GATE-Pad8) -> GND
- U11 pad 9: /Charge OR-ing/IN -> /Solar Charger/MPPT1/FB
- U12 pad 13: /PGOOD1 -> /Solar Charger/PGOOD3
- U12 pad 14: /Charge OR-ing/IN -> /Solar Charger/Charge OR-ing2/IN
- U12 pad 2: VSOLAR -> /Solar Charger/MPPT2/VIN
- U12 pad 3: VSOLAR -> /Solar Charger/MPPT2/VIN
- U12 pad 4: VSOLAR -> /Solar Charger/MPPT2/RUN
- U12 pad 5: /MPPT/VCC -> /Solar Charger/MPPT2/VCC
- U12 pad 6: /MPPT/MPPC -> /Solar Charger/MPPT2/MPPC
- U12 pad 9: /MPPT/FB -> /Solar Charger/MPPT2/FB
- U13 pad 1: /Charge OR-ing2/IN -> VBATT
- U13 pad 10: /Charge OR-ing2/IN -> unconnected-(U13-GATE-Pad10)
- U13 pad 2: /Charge OR-ing2/IN -> /Solar Charger/VCHRG
- U13 pad 3: /Charge OR-ing2/IN -> Net-(U13-ON)
- U13 pad 4: /Charge OR-ing2/IN -> GND
- U13 pad 5: (no net) -> Net-(U13-TIMER)
- U13 pad 6: GND -> /Solar Charger/I2C Single Protection5/DEVICE
- U13 pad 7: VCHRG -> /Solar Charger/I2C Single Protection4/DEVICE
- U13 pad 8: unconnected-(U13-GATE-Pad8) -> /Solar Charger/A0_S
- U13 pad 9: /Charge OR-ing2/IN -> /Solar Charger/A1_S
- U2 pad 1: VBATT -> /Coil Driver/IPROPI
- U2 pad 10: unconnected-(U2-GATE-Pad10) -> /Coil Driver/A0_COIL
- U2 pad 2: VDRIVE -> unconnected-(U2-RSVD-Pad2)
- U2 pad 3: Net-(U2-ON) -> unconnected-(U2-RSVD-Pad3)
- U2 pad 4: GND -> Net-(U2-NFAULT)
- U2 pad 5: Net-(U2-TIMER) -> /Coil Driver/VM
- U2 pad 6: SCL_CPWR -> COIL_P
- U2 pad 7: SDA_CPWR -> GND
- U2 pad 8: Net-(U2-A0) -> COIL_N
- U2 pad 9: GND -> /Coil Driver/A1_COIL
- U3 pad 1: Net-(U3-BST1) -> Net-(D6-A)
- U3 pad 2: D_VSOLAR1 -> Net-(D6-A)
- U3 pad 3: D_VSOLAR1 -> Net-(D6-A)
- U3 pad 4: D_VSOLAR1 -> Net-(U1-GATE)
- U3 pad 5: /MPPT1/VCC -> /Solar Charger/VCHRG
- U4 pad 1: Net-(U4-BST1) -> Net-(D7-A)
- U4 pad 2: D_VSOLAR2 -> GND
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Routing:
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- added copper zone on B.Cu, net /Coil Driver/VM
- added copper zone on B.Cu, net /Solar Charger/Charge OR-ing/IN
- added copper zone on B.Cu, net /Solar Charger/Charge OR-ing1/IN
- added copper zone on B.Cu, net /Solar Charger/Charge OR-ing2/IN
- added copper zone on B.Cu, net /Solar Charger/MPPT1/VIN
- added copper zone on B.Cu, net /Solar Charger/MPPT2/VIN
- added copper zone on B.Cu, net /Solar Charger/VCHRG
- added copper zone on B.Cu, net /Solar Charger/VSOLAR
- added copper zone on In1.Cu, net GND
- added copper zone on In2.Cu, net MAIN_3V3
- added copper zone on B.Cu, net Net-(D8-A)
- added copper zone on B.Cu, net Net-(F2-Pad1)
- added copper zone on B.Cu, net Net-(U10-BST1)
- added copper zone on B.Cu, net Net-(U10-BST2)
- added copper zone on B.Cu, net Net-(U10-SW1)
- added copper zone on B.Cu, net Net-(U10-SW2)
- added copper zone on B.Cu, net Net-(U11-BST1)
- added copper zone on B.Cu, net Net-(U11-BST2)
- added copper zone on B.Cu, net Net-(U11-SW1)
- added copper zone on B.Cu, net Net-(U11-SW2)
- removed copper zone on B.Cu, net +5V
- removed copper zone on B.Cu, net /Charge OR-ing/IN
- removed copper zone on B.Cu, net /Charge OR-ing1/IN
- removed copper zone on B.Cu, net /Charge OR-ing2/IN
- removed copper zone on B.Cu, net /MPPT/VCC
- removed copper zone on B.Cu, net /MPPT1/VCC
- removed copper zone on B.Cu, net /MPPT2/VCC
- removed copper zone on B.Cu, net 3.3V
- removed copper zone on In1.Cu, net 3.3V
- removed copper zone on B.Cu, net D_VSOLAR1
- removed copper zone on B.Cu, net D_VSOLAR2
- removed copper zone on In2.Cu, net GND
- removed copper zone on B.Cu, net Net-(D10-K)
- removed copper zone on B.Cu, net Net-(D11-A)
- removed copper zone on B.Cu, net Net-(U12-EXTVCC)
- removed copper zone on B.Cu, net Net-(U3-BST1)
- removed copper zone on B.Cu, net Net-(U3-BST2)
- removed copper zone on B.Cu, net Net-(U3-EXTVCC)
- removed copper zone on B.Cu, net Net-(U3-SW1)
- removed copper zone on B.Cu, net Net-(U3-SW2)
- removed copper zone on B.Cu, net Net-(U4-BST1)
- removed copper zone on B.Cu, net Net-(U4-BST2)
- removed copper zone on B.Cu, net Net-(U4-EXTVCC)
- removed copper zone on B.Cu, net Net-(U4-SW1)
- removed copper zone on B.Cu, net Net-(U4-SW2)
- removed copper zone on B.Cu, net VCHRG
- removed copper zone on B.Cu, net VDRIVE
- removed copper zone on B.Cu, net VSOLAR
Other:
- board text removed: "+"
- board text removed: "-"
- board text removed: "Charge Sense"
- board text removed: "Coil Power Sense"
- board text removed: "D VSOLAR 1"
- board text removed: "D VSOLAR 2"
- board text removed: "I2C BUS PROTECTION"
- board text removed: "MPPT"
- board text removed: "OR-ing"
- board text removed: "SCL CHARGE SENSE"
- board text removed: "SCL COIL DRIVER"
- board text removed: "SCL COIL POW"
- board text removed: "SCL LS"
- board text removed: "SDA CHARGE SENSE"
- board text removed: "SDA COIL DRIVER"
- board text removed: "SDA COIL POW"
- board text removed: "SDA LS"
- board text removed: "VSOLAR"

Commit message: almost done
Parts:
- added SC6: SM141K06L, Argus-Miscellaneous:SM141K06TF, F.Cu at (152.4, 128.3)
- H1, H2, H3, H4: footprint SolarPanels:MountingHole_3.2mm_M3_DIN965_Pad_TopBottom -> MountingHole:MountingHole_3.2mm_M3_DIN965_Pad_TopBottom
- H5, H6: footprint SolarPanels:MountingHole_3mm -> MountingHole:MountingHole_3mm
- R54: value 0R -> 1k
- SC1, SC2, SC4, SC5: value SM141K06TF -> SM141K06L; footprint SolarPanels:SM141K06TF -> Argus-Miscellaneous:SM141K06TF
- SC3: footprint SolarPanels:SM141K10TF -> Argus-Miscellaneous:SM141K10TF
- U2: footprint SolarPanels:WQFN16_RTE_TEX -> Argus-IC:WQFN16_RTE_TEX
- U5: footprint SolarPanels:OPT4003 -> Argus-IC:OPT4003
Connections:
- J2 pad 3: MAIN_3V3 -> COIL_DRIVER_EN
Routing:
- net COIL_DRIVER_EN: track 5.07 -> 32.3 mm, vias 0 -> 2
- net Net-(D3-K): track 143.5 -> 134.9 mm
- net Net-(D2-K): track 61.8 -> 67.7 mm
- net GND: track 130.4 -> 136.1 mm
- net Net-(D4-K): track 52.2 -> 55.2 mm
- net /Solar Charger/I2C Single Protection5/DEVICE: track 24.8 -> 27.2 mm
- net Net-(D1-K): track 52.2 -> 54.4 mm
- net MAIN_3V3: track 40.6 -> 38.4 mm
- net SDA: track 122.7 -> 124.2 mm, vias 4 -> 3
- net Net-(D5-K): track 34.4 -> 33.5 mm
